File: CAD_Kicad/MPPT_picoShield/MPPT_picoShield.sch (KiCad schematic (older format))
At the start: 43 parts, among them J1 PV_input, J2 Battery_pack, J3 V_out, Q1 Q_PMOS_GDS, SW1 RESET, U1 RaspiPico

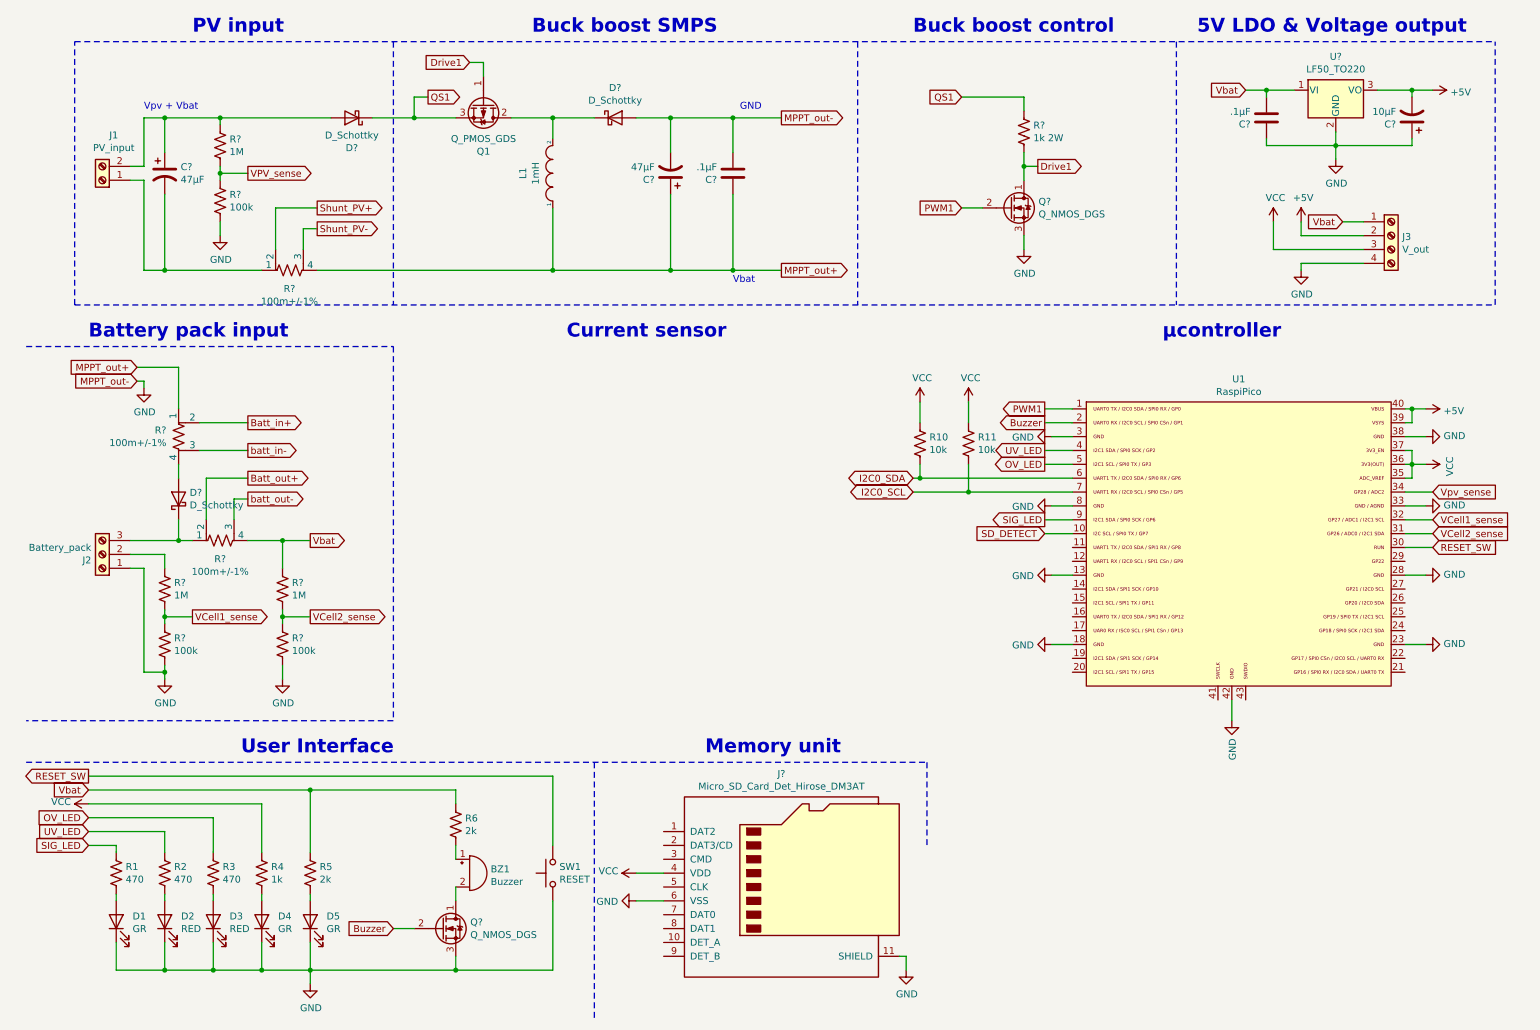
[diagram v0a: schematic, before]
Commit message: Finished electrical schematic - pending review
Final decisions on component choices have to be made, special attention should be put towards the microSD card (there seems to be a conflict between electrical schematic and footprint gathered on the internet). Power components in the SMPS (caps and inductors) have yet to be chosen
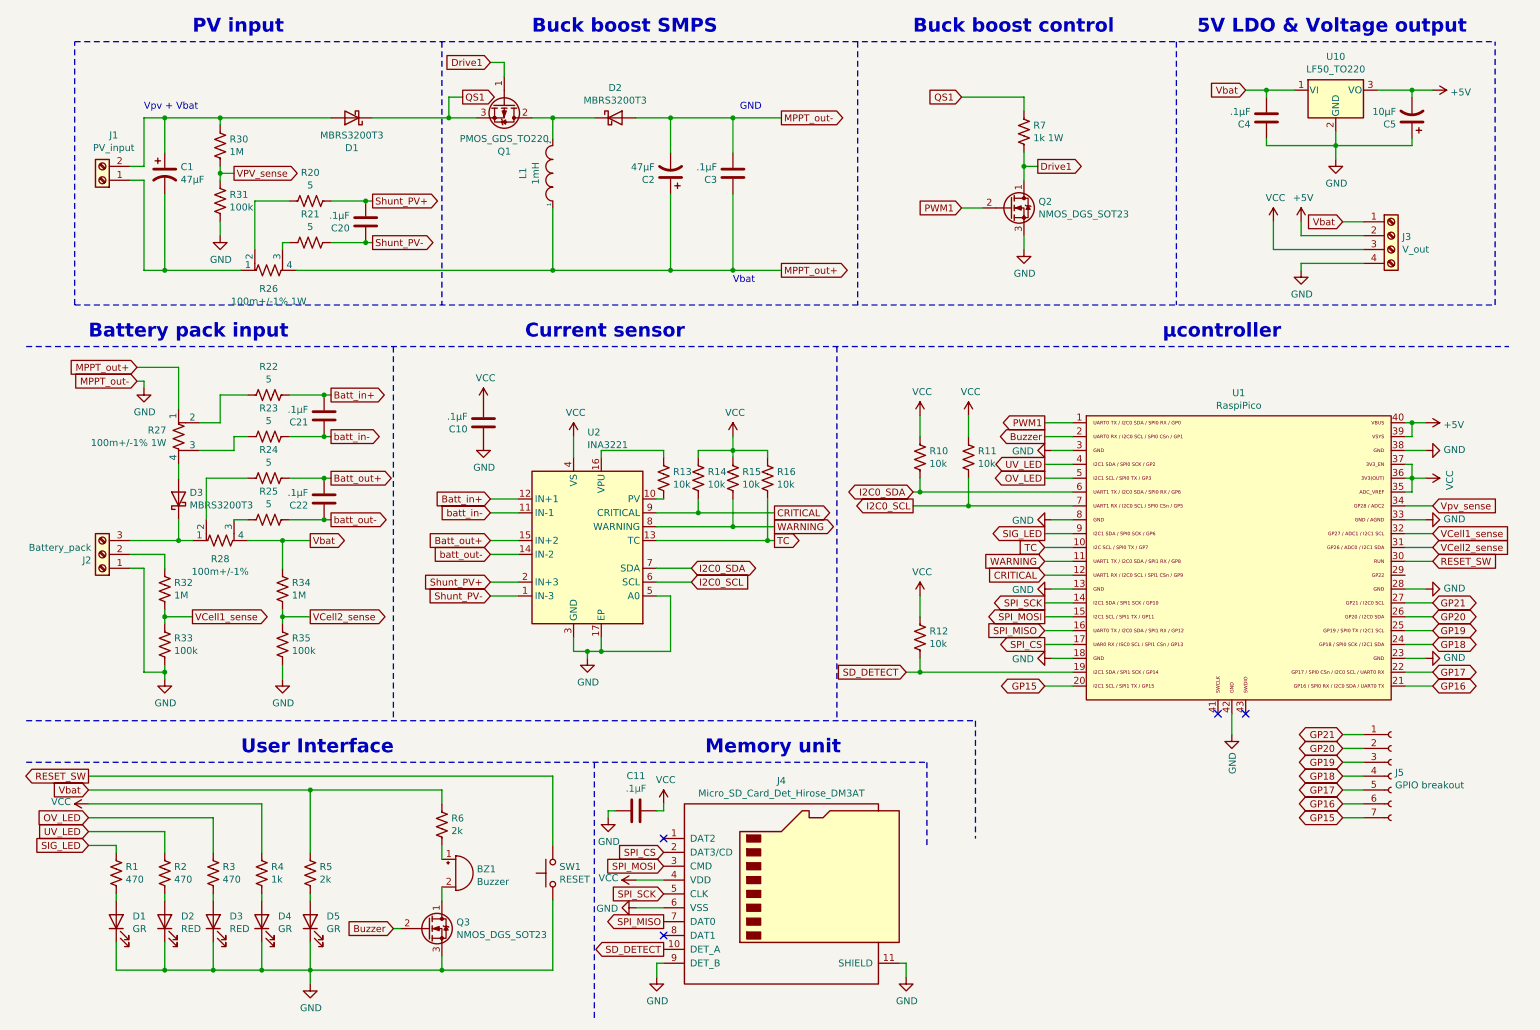
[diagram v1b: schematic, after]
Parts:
- added C10, C11, C20, C21, C22: .1µF, Capacitor_SMD:C_0603_1608Metric, symbol Device:C
- added J5: GPIO breakout, Connector_PinHeader_2.54mm:PinHeader_1x07_P2.54mm_Vertical, symbol Connector:Conn_01x07_Female
- added R12, R13, R14, R15, R16: 10k, Resistor_SMD:R_0603_1608Metric, symbol Device:R_US
- added R20, R21, R22, R23, R24, R25: 5, Resistor_SMD:R_0603_1608Metric, symbol Device:R_US
- added U2: INA3221, Package_DFN_QFN:Texas_RGV_S-PVQFN-N16_EP2.1x2.1mm, symbol Power_Management:INA3221
- BZ1: footprint (none) -> Custom_MPPT:PKM13EPYH4002-B0
- C3, C4: renamed from C?; footprint (none) -> Capacitor_SMD:C_0603_1608Metric
- D1, D2, D3: renamed from D?; value D_Schottky -> MBRS3200T3; footprint (none) -> Custom_MPPT:MBRS3200T3G
- D1, D2, D3, D4, D5: footprint (none) -> LED_SMD:LED_0805_2012Metric
- J1: footprint (none) -> TerminalBlock:TerminalBlock_bornier-2_P5.08mm
- J2: footprint (none) -> TerminalBlock:TerminalBlock_bornier-3_P5.08mm
- J3: footprint (none) -> TerminalBlock:TerminalBlock_bornier-4_P5.08mm
- J4: renamed from J?; footprint (none) -> Custom_MPPT:DM3ATSFPEJM5
- Q1: value Q_PMOS_GDS -> PMOS_GDS_TO220; footprint (none) -> Package_TO_SOT_THT:TO-220-3_Vertical
- Q2, Q3: renamed from Q?; value Q_NMOS_DGS -> NMOS_DGS_SOT23; footprint (none) -> Package_TO_SOT_SMD:SOT-23
- R26, R27: renamed from R?; value 100m+/-1% -> 100m+/-1% 1W; footprint (none) -> Resistor_SMD:R_1206_3216Metric
- R28: renamed from R?; footprint (none) -> Resistor_SMD:R_1206_3216Metric
- R7: renamed from R?; value 1k 2W -> 1k 1W; footprint Resistor_SMD:R_0603_1608Metric -> Resistor_SMD:R_1206_3216Metric
- gave numbers to parts that had none: 10
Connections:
- net Batt_in+: now also C21.2, R22.1, U2.12 (IN+1); no longer R27.2
- net Batt_out+: now also C22.2, R24.1, U2.15 (IN+2); no longer R28.2
- net GND: now also J4.9 (DET_B), C10.1, C11.2, U2.17 (EP), U2.3 (GND), U2.5 (A0)
- net I2C0_SCL: now also U2.6 (SCL)
- net I2C0_SDA: now also U2.7 (SDA)
- net SD_DETECT: now also J4.10 (DET_A), U1.19, R12.2; no longer U1.10
- net Shunt_PV+: now also C20.2, R20.1, U2.2 (IN+3); no longer R26.2
- net Shunt_PV-: now also C20.1, R21.1, U2.1 (IN-3); no longer R26.3
- net VCC: now also C10.2, C11.1, R12.1, R14.1, R15.1, R16.1, U2.4 (VS)
- net batt_in-: now also C21.1, R23.1, U2.11 (IN-1); no longer R27.3
- net batt_out-: now also C22.1, R25.1, U2.14 (IN-2); no longer R28.3
- net WARNING: now reaches U1.11
- net WARNING: now also R15.2, U2.8 (WARNING)
- net CRITICAL: now reaches U1.12
- net CRITICAL: now also R14.2, U2.9 (CRITICAL)
- net SPI_SCK: now reaches U1.14
- net SPI_SCK: now also J4.5 (CLK)
- net SPI_MOSI: now reaches U1.15
- net SPI_MOSI: now also J4.3 (CMD)
- net SPI_MISO: now reaches U1.16
- net SPI_MISO: now also J4.7 (DAT0)
- net SPI_CS: now reaches U1.17
- net SPI_CS: now also J4.2 (DAT3/CD)
- net GP15: now reaches U1.20
- net GP15: now also J5.7 (Pin_7)
- net GP16: now reaches U1.21
- net GP16: now also J5.6 (Pin_6)
- net GP17: now reaches U1.22
- net GP17: now also J5.5 (Pin_5)
- net GP18: now reaches U1.24
- net GP18: now also J5.4 (Pin_4)
- net GP19: now reaches U1.25
- net GP19: now also J5.3 (Pin_3)
- net GP20: now reaches U1.26
- net GP20: now also J5.2 (Pin_2)
- net GP21: now reaches U1.27
- net GP21: now also J5.1 (Pin_1)
- new net: R13.2, U2.10 (PV)
- new net: R13.1, U2.16 (VPU)
- new net: R20.2, R26.2
- new net: R21.2, R26.3
- new net: R24.2, R28.2
- new net: R25.2, R28.3
- new net: R22.2, R27.2
- new net: R23.2, R27.3
- new net TC: R16.2, U1.10, U2.13 (TC)
- no-connect marks 0 -> 4
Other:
- moved on the sheet: BZ1, J4, Q1, Q3, R10, R11, R26, R6, U1

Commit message: Initial placement of components on PCB board
Initial placement - issue spotted on shunt resistors: hard to route because of crossing, pending solution
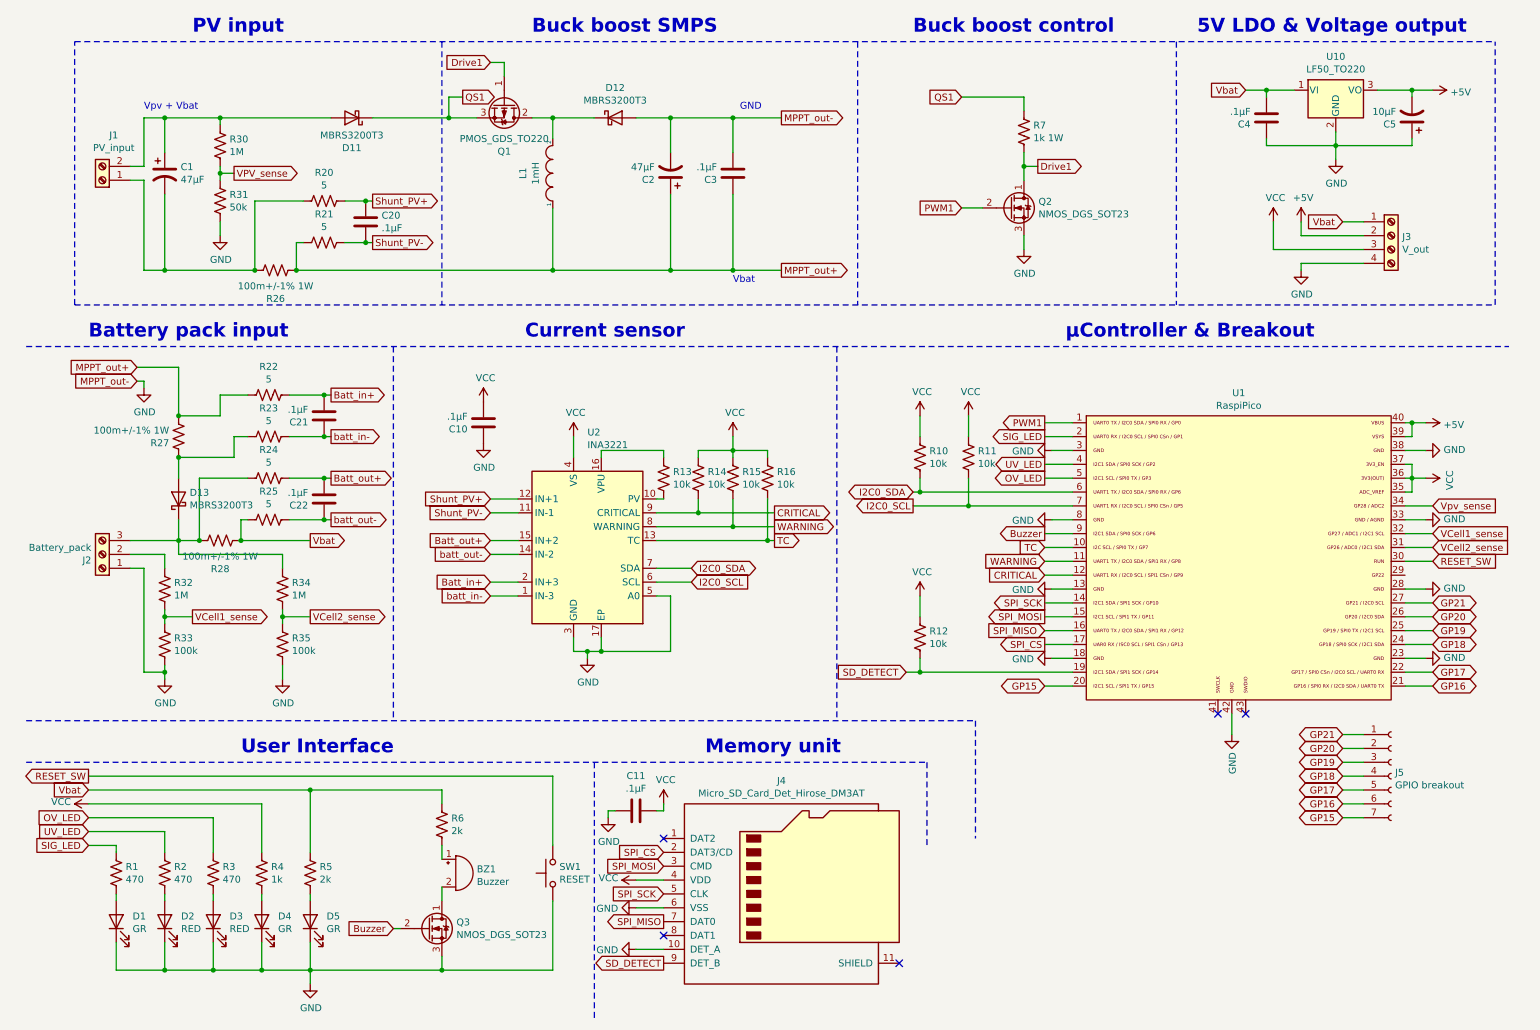
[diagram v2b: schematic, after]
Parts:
- removed R26, R27: 100m+/-1% 1W, Resistor_SMD:R_1206_3216Metric, symbol Device:R_Shunt_US
- removed R28: 100m+/-1%, Resistor_SMD:R_1206_3216Metric, symbol Device:R_Shunt_US
- added R26, R27, R28: 100m+/-1% 1W, Resistor_SMD:R_1206_3216Metric, symbol Device:R_US
- C1, C2, C5: footprint (none) -> Capacitor_THT:CP_Radial_D10.0mm_P5.00mm
- L1: footprint (none) -> Custom_MPPT:PA4320.105NLT
- R31: value 100k -> 50k
- SW1: footprint (none) -> Button_Switch_THT:SW_PUSH_6mm
- renumbered D1 to D11, D2 to D12, D3 to D13
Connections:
- net Batt_in+: now also U2.2 (IN+3); no longer U2.12 (IN+1)
- net Buzzer: now also U1.9; no longer U1.2
- net GND: now also J4.10 (DET_A); no longer J4.11 (SHIELD), J4.9 (DET_B)
- net MPPT_out+: now also R21.2, R22.2, R26.2, R27.2
- net SD_DETECT: now also J4.9 (DET_B); no longer J4.10 (DET_A)
- net SIG_LED: now also U1.2; no longer U1.9
- net Shunt_PV+: now also C20.1, U2.12 (IN+1); no longer C20.2, U2.2 (IN+3)
- net Shunt_PV-: now also C20.2, U2.11 (IN-1); no longer C20.1, U2.1 (IN-3)
- net Vbat: now also R25.2, R28.2; no longer R34.1
- net batt_in-: now also U2.1 (IN-3); no longer U2.11 (IN-1)
- net at C1.2, J1.1 (Pin_1): now also R20.2, R26.1
- net at D13.1 (K), J2.3 (Pin_3): now also R24.2, R34.1, R28.1
- net at R23.2: now also D13.2 (A), R27.1
- no-connect marks 4 -> 5
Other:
- note added: "µController & Breakout"
- note removed: "µcontroller"
- moved on the sheet: R20, R21
